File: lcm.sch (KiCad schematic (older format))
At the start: 13 parts, among them J6 F52R-1A7H1-11020, U11 NTS0102GT

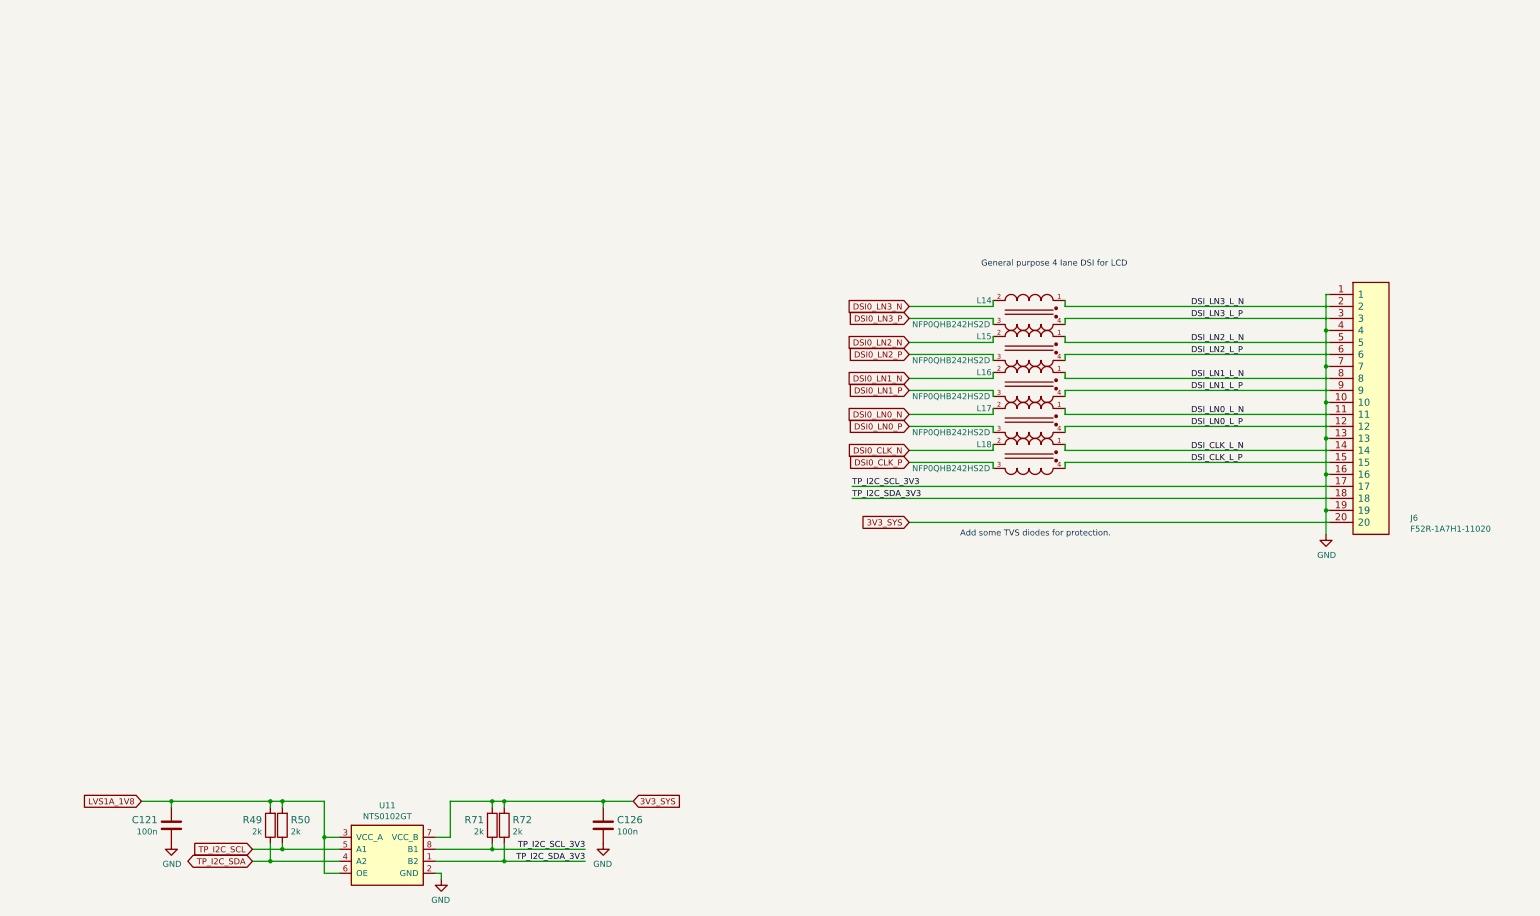
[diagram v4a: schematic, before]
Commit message: Reorganize schematics, add descriptions in top left corner
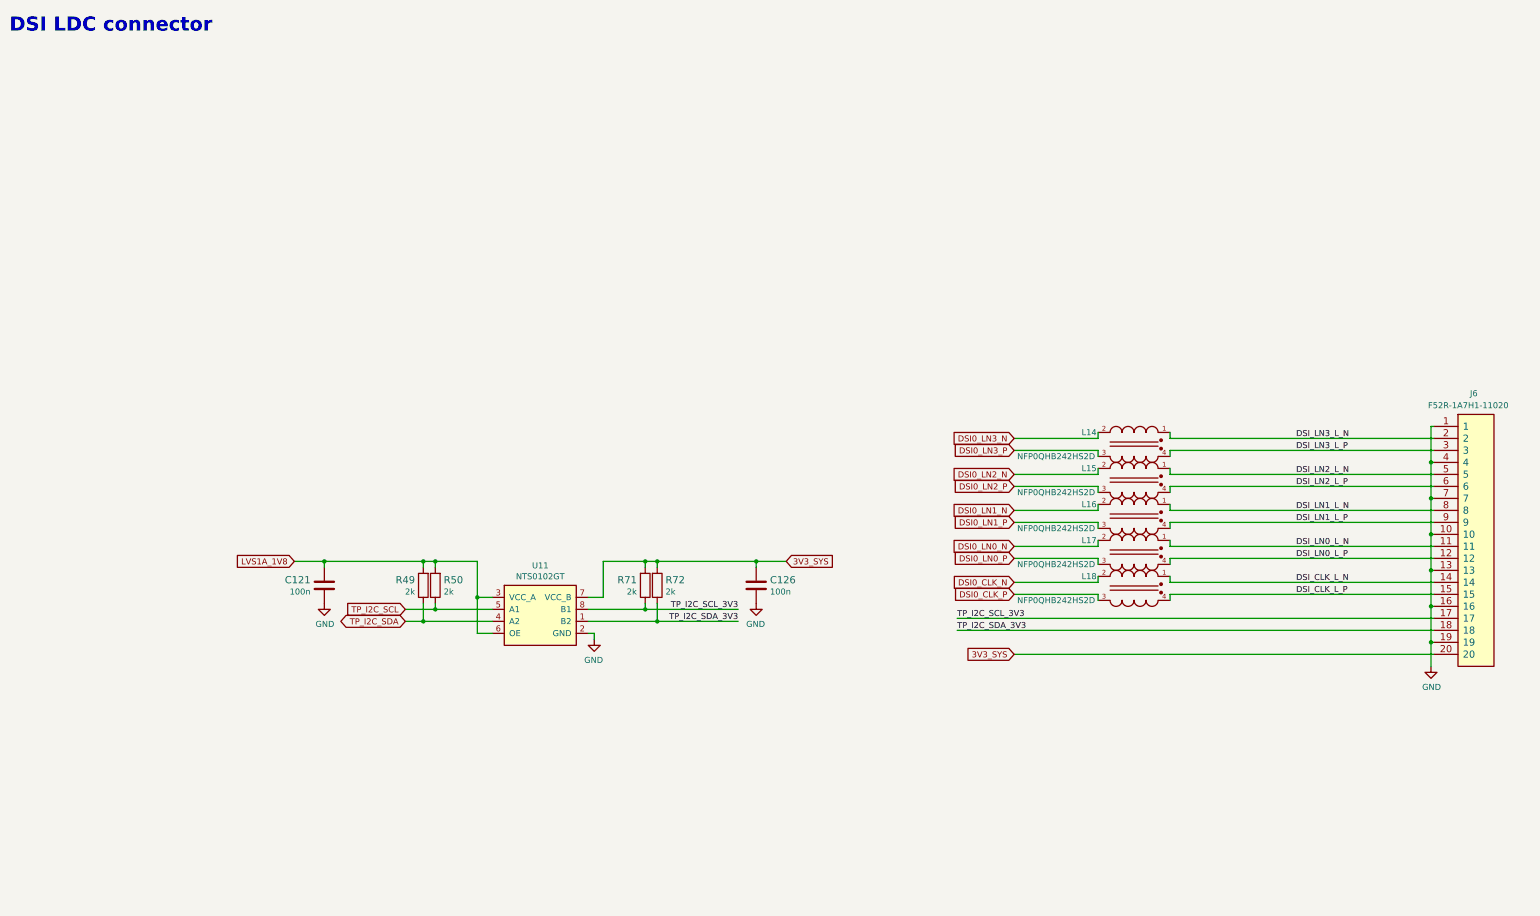
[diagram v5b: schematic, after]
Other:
- note added: "DSI LDC connector"
- note removed: "Add some TVS diodes for protection."
- note removed: "General purpose 4 lane DSI for LCD"
- moved on the sheet: C121, C126, J6, L14, L15, L16, L17, L18, R49, R50, R71, R72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

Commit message: Clear annotation and annotate
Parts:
- renumbered C121 to C97, C126 to C98, L14 to L11, L15 to L12, L16 to L13, L17 to L14, L18 to L15, R49 to R65, R50 to R66, R71 to R67, R72 to R68, U11 to U10
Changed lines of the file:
@@
 Connection ~ 12375 5800
 $Comp
-L sa800u-baseboard-hw:GND #PWR066
+L sa800u-baseboard-hw:GND #PWR085
 U 1 1 61BEA7A9
 P 12375 6000
-F 0 "#PWR066" H 12375 5750 50  0001 C CNN
+F 0 "#PWR085" H 12375 5750 50  0001 C CNN
 F 1 "GND" H 12380 5827 50  0000 C CNN
 F 2 "" H 12375 6000 50  0001 C CNN
@@
 P 9900 4450
 AR Path="/61C82351" Ref="L?"  Part="1"
-AR Path="/61BD2CC1/61C82351" Ref="L15"  Part="1"
-F 0 "L15" H 10275 4550 50  0000 C CNN
+AR Path="/61BD2CC1/61C82351" Ref="L12"  Part="1"
+F 0 "L12" H 10275 4550 50  0000 C CNN
 F 1 "NFP0QHB242HS2D" H 10550 4350 50  0000 C CNN
 F 2 "sa800u-baseboard-hw-footprints:FIL_NFP0QHB242HS2D" H 9900 4450 50  0001 C CNN
@@
 P 9900 4750
 AR Path="/61C82CCB" Ref="L?"  Part="1"
-AR Path="/61BD2CC1/61C82CCB" Ref="L16"  Part="1"
-F 0 "L16" H 10275 4850 50  0000 C CNN
+AR Path="/61BD2CC1/61C82CCB" Ref="L13"  Part="1"
+F 0 "L13" H 10275 4850 50  0000 C CNN
 F 1 "NFP0QHB242HS2D" H 10550 4650 50  0000 C CNN
 F 2 "sa800u-baseboard-hw-footprints:FIL_NFP0QHB242HS2D" H 9900 4750 50  0001 C CNN
@@
 P 9900 5050
 AR Path="/61C832C1" Ref="L?"  Part="1"
-AR Path="/61BD2CC1/61C832C1" Ref="L17"  Part="1"
-F 0 "L17" H 10275 5150 50  0000 C CNN
+AR Path="/61BD2CC1/61C832C1" Ref="L14"  Part="1"
+F 0 "L14" H 10275 5150 50  0000 C CNN
 F 1 "NFP0QHB242HS2D" H 10550 4950 50  0000 C CNN
 F 2 "sa800u-baseboard-hw-footprints:FIL_NFP0QHB242HS2D" H 9900 5050 50  0001 C CNN
@@
 P 9900 5350
 AR Path="/61C83C74" Ref="L?"  Part="1"
-AR Path="/61BD2CC1/61C83C74" Ref="L18"  Part="1"
-F 0 "L18" H 10275 5450 50  0000 C CNN
+AR Path="/61BD2CC1/61C83C74" Ref="L15"  Part="1"
+F 0 "L15" H 10275 5450 50  0000 C CNN
 F 1 "NFP0QHB242HS2D" H 10550 5250 50  0000 C CNN
 F 2 "sa800u-baseboard-hw-footprints:FIL_NFP0QHB242HS2D" H 9900 5350 50  0001 C CNN
@@
 3V3_SYS
 $Comp
-L sa800u-baseboard-hw:NTS0102GT U11
+L sa800u-baseboard-hw:NTS0102GT U10
 U 1 1 65E71148
 P 4950 5675
-F 0 "U11" H 4950 6190 50  0000 C CNN
+F 0 "U10" H 4950 6190 50  0000 C CNN
 F 1 "NTS0102GT" H 4950 6099 50  0000 C CNN
 F 2 "sa800u-baseboard-hw-footprints:PSON50P100X195X50-8N" H 4850 6175 50  0001 C CNN
@@
 3V3_SYS
 $Comp
-L sa800u-baseboard-hw:C_100n_0402 C121
+L sa800u-baseboard-hw:C_100n_0402 C97
 U 1 1 660118DD
 P 3150 5325
-F 0 "C121" H 3035 5370 60  0000 R CNN
+F 0 "C97" H 3035 5370 60  0000 R CNN
 F 1 "C_100n_0402" H 3150 5175 60  0001 C CNN
 F 2 "sa800u-baseboard-hw-footprints:0402-cap" H 3350 5525 60  0001 L CNN
@@
 	3150 5125 3150 5175
 $Comp
-L sa800u-baseboard-hw:GND #PWR0166
+L sa800u-baseboard-hw:GND #PWR082
 U 1 1 66028DF2
 P 3150 5475
-F 0 "#PWR0166" H 3150 5225 50  0001 C CNN
+F 0 "#PWR082" H 3150 5225 50  0001 C CNN
 F 1 "GND" H 3155 5302 50  0000 C CNN
 F 2 "" H 3150 5475 50  0001 C CNN
@@
 $EndComp
 $Comp
-L sa800u-baseboard-hw:R_2k_0402 R50
+L sa800u-baseboard-hw:R_2k_0402 R66
 U 1 1 6605EB55
 P 4075 5325
-F 0 "R50" V 4120 5255 60  0000 R CNN
+F 0 "R66" V 4120 5255 60  0000 R CNN
 F 1 "R_2k_0402" H 4075 5175 60  0001 C CNN
 F 2 "sa800u-baseboard-hw-footprints:0402-res" H 4275 5525 60  0001 L CNN
@@
 	5475 5425 5350 5425
 $Comp
-L sa800u-baseboard-hw:C_100n_0402 C126
+L sa800u-baseboard-hw:C_100n_0402 C98
 U 1 1 660892B3
 P 6750 5325
-F 0 "C126" H 6635 5370 60  0000 R CNN
+F 0 "C98" H 6635 5370 60  0000 R CNN
 F 1 "C_100n_0402" H 6750 5175 60  0001 C CNN
 F 2 "sa800u-baseboard-hw-footprints:0402-cap" H 6950 5525 60  0001 L CNN
@@
 	6750 5125 6750 5175
 $Comp
-L sa800u-baseboard-hw:GND #PWR0167
+L sa800u-baseboard-hw:GND #PWR084
 U 1 1 660892BB
 P 6750 5475
-F 0 "#PWR0167" H 6750 5225 50  0001 C CNN
+F 0 "#PWR084" H 6750 5225 50  0001 C CNN
 F 1 "GND" H 6755 5302 50  0000 C CNN
 F 2 "" H 6750 5475 50  0001 C CNN
@@
 	5475 5125 5475 5425
 $Comp
-L sa800u-baseboard-hw:GND #PWR0168
+L sa800u-baseboard-hw:GND #PWR083
 U 1 1 660AB186
 P 5400 5775
-F 0 "#PWR0168" H 5400 5525 50  0001 C CNN
+F 0 "#PWR083" H 5400 5525 50  0001 C CNN
 F 1 "GND" H 5405 5602 50  0000 C CNN
 F 2 "" H 5400 5775 50  0001 C CNN
@@
 	3975 5475 3975 5625
 $Comp
-L sa800u-baseboard-hw:R_2k_0402 R49
+L sa800u-baseboard-hw:R_2k_0402 R65
 U 1 1 6605EB4C
 P 3975 5325
-F 0 "R49" V 4020 5394 60  0000 L CNN
+F 0 "R65" V 4020 5394 60  0000 L CNN
 F 1 "R_2k_0402" H 3975 5175 60  0001 C CNN
 F 2 "sa800u-baseboard-hw-footprints:0402-res" H 4175 5525 60  0001 L CNN
@@
 	5825 5475 5825 5525
 $Comp
-L sa800u-baseboard-hw:R_2k_0402 R71
+L sa800u-baseboard-hw:R_2k_0402 R67
 U 1 1 660892CF
 P 5825 5325
-F 0 "R71" V 5870 5255 60  0000 R CNN
+F 0 "R67" V 5870 5255 60  0000 R CNN
 F 1 "R_2k_0402" H 5825 5175 60  0001 C CNN
 F 2 "sa800u-baseboard-hw-footprints:0402-res" H 6025 5525 60  0001 L CNN
@@
 $EndComp
 $Comp
-L sa800u-baseboard-hw:R_2k_0402 R72
+L sa800u-baseboard-hw:R_2k_0402 R68
 U 1 1 660892C6
 P 5925 5325
-F 0 "R72" V 5970 5394 60  0000 L CNN
+F 0 "R68" V 5970 5394 60  0000 L CNN
 F 1 "R_2k_0402" H 5925 5175 60  0001 C CNN
 F 2 "sa800u-baseboard-hw-footprints:0402-res" H 6125 5525 60  0001 L CNN
@@
 P 9900 4150
 AR Path="/61C65B0C" Ref="L?"  Part="1"
-AR Path="/61BD2CC1/61C65B0C" Ref="L14"  Part="1"
-F 0 "L14" H 10275 4250 50  0000 C CNN
+AR Path="/61BD2CC1/61C65B0C" Ref="L11"  Part="1"
+F 0 "L11" H 10275 4250 50  0000 C CNN
 F 1 "NFP0QHB242HS2D" H 10550 4050 50  0000 C CNN
 F 2 "sa800u-baseboard-hw-footprints:FIL_NFP0QHB242HS2D" H 9900 4150 50  0001 C CNN
